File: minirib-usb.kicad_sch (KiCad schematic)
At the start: 49 parts, among them J1 USB_B_Micro, J2 Mini-DIN-6-Shielded, J3 UART, J4 UART, Q1 BS84W, Q2 BS84W, Q3 BSS138W, Q4 BS84W, Q5 BSS138W, Q6 BSS138W, Q7 BSS138W, U1 FT231XS, U2 TL071

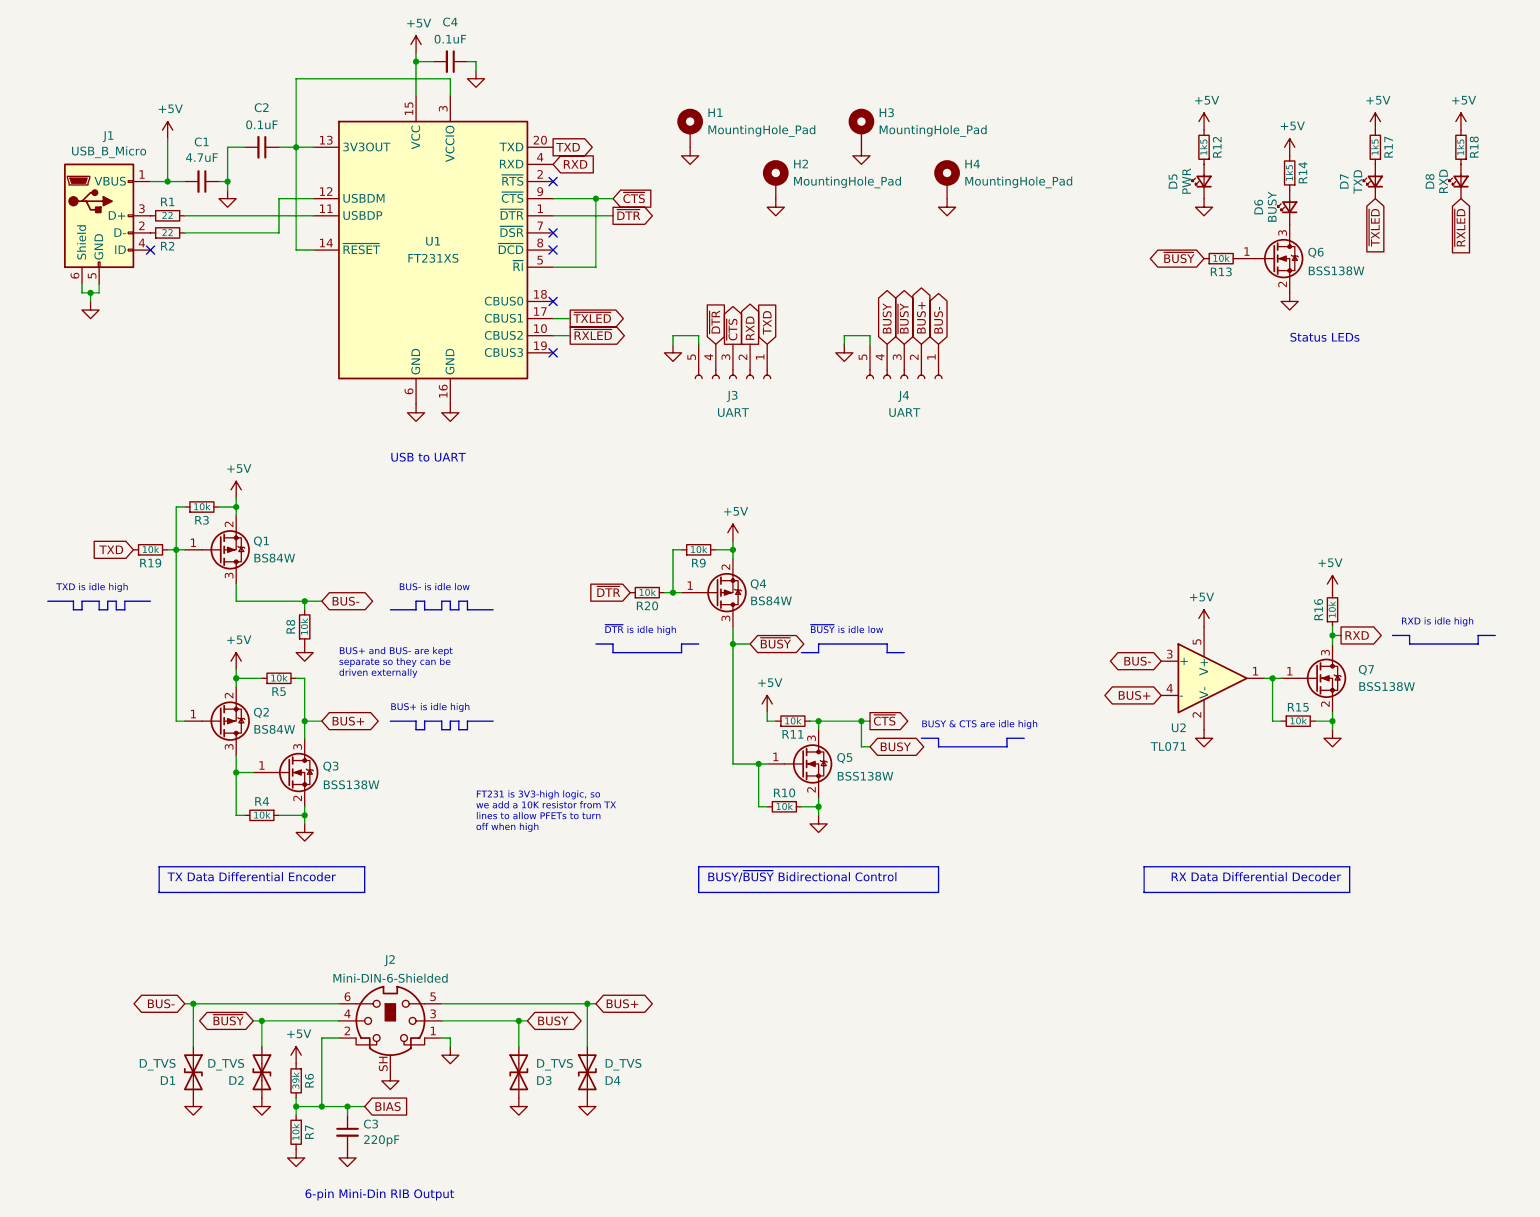
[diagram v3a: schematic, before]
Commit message: PCB assembly updates
updates to revision E to add LCSC components to allow for JLCPCB manufacture
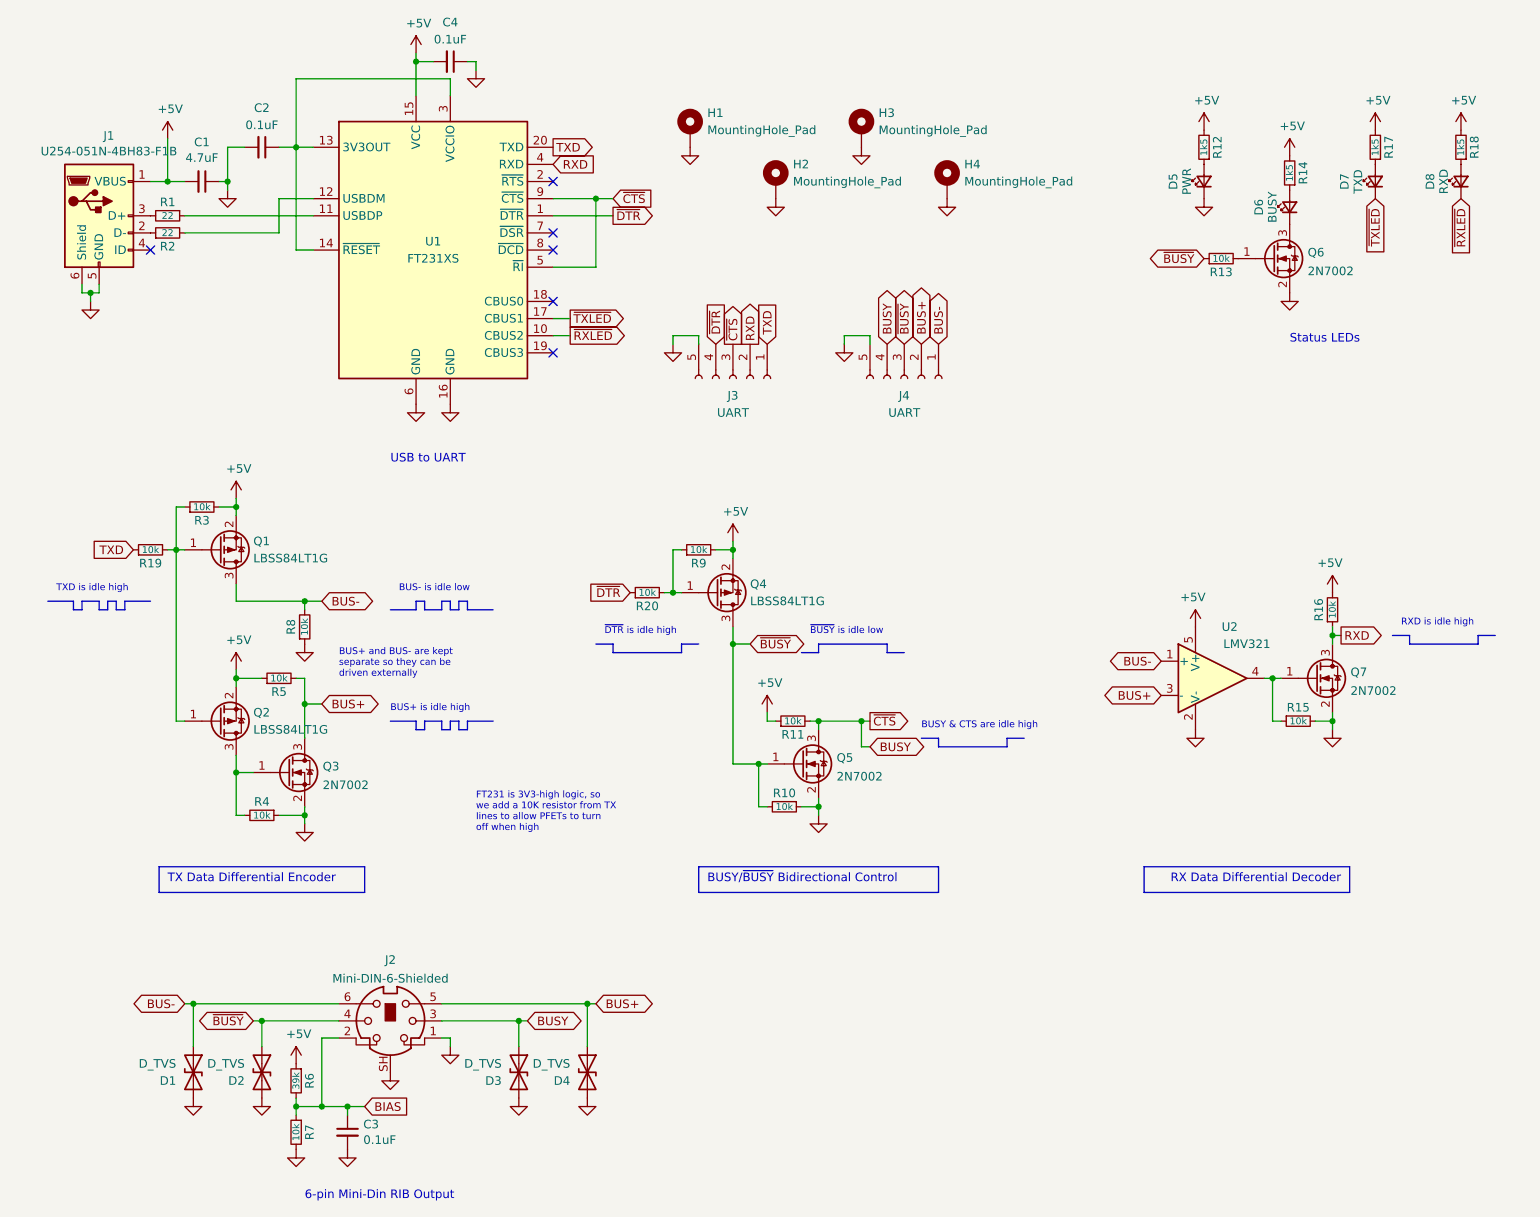
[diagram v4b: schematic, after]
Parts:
- removed U2: TL071, Package_TO_SOT_SMD:SOT-23-5_HandSoldering, symbol MiniDin:TL071
- added U2: LMV321, Package_TO_SOT_SMD:SOT-23-5_HandSoldering, symbol Amplifier_Operational:LMV321
- C1: LCSC (none) -> C1779
- C2, C4: LCSC (none) -> C49678
- C3: value 220pF -> 0.1uF; LCSC (none) -> C49678
- D1, D2, D3, D4: footprint Diode_SMD:D_0805_2012Metric_Pad1.15x1.40mm_HandSolder -> Diode_SMD:D_SOD-123F; LCSC (none) -> C2990473
- D5: LCSC (none) -> C434433
- D6: LCSC (none) -> C2296
- D7: LCSC (none) -> C84256
- D8: LCSC (none) -> C434435
- J1: value USB_B_Micro -> U254-051N-4BH83-F1B; footprint Connector_USB:USB_Micro-B_Wuerth_629105150521 -> lcsc-comps:U254-051N-4BH83-F1B; LCSC (none) -> C319169
- Q1, Q2, Q4: value BS84W -> LBSS84LT1G; footprint Package_TO_SOT_SMD:SOT-323_SC-70_Handsoldering -> Package_TO_SOT_SMD:SOT-23_Handsoldering; LCSC (none) -> C8492
- Q3, Q5, Q6, Q7: value BSS138W -> 2N7002; footprint Package_TO_SOT_SMD:SOT-323_SC-70_Handsoldering -> Package_TO_SOT_SMD:SOT-23_Handsoldering; LCSC (none) -> C8545
- R10, R11, R13, R15, R16, R19, R20, R3, R4, R5, R7, R8, R9: LCSC (none) -> C17414
- R12, R14, R17, R18: LCSC (none) -> C4310
- R6: LCSC (none) -> C25826
- U1: LCSC (none) -> C132160
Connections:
- net +5V: now also U2.5 (V+)
- net BUS+: now also U2.3 (-)
- net BUS-: now also U2.1 (+)
- net GND: now also U2.2 (V-)
- net at Q7.1 (G), R15.1: now also U2.4
